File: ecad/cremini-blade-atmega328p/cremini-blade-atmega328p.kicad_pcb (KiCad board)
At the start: 2 copper layers, 25 x 99 mm, 96 parts, among them J1 USB-C PORT, J2 ICSP, J3 BACKPLANE, J4 RASPBERRY PI GPIO, Q1 AO3400A, Q2 AO3400A, Q3 SI2301CDS-T1-GE3, Q4 AO3400A, SW1 RESET, SW2 SW_DIP_x06, U1 ACS712ELCTR-20A-T, U2 ACS712ELCTR-20A-T, U3 LM358D, U4 CH340G, U5 AMS1117-3.3, U6 ATMEGA328P-AU, U7 74HC244D, Y1 12MHz, Y2 16MHz

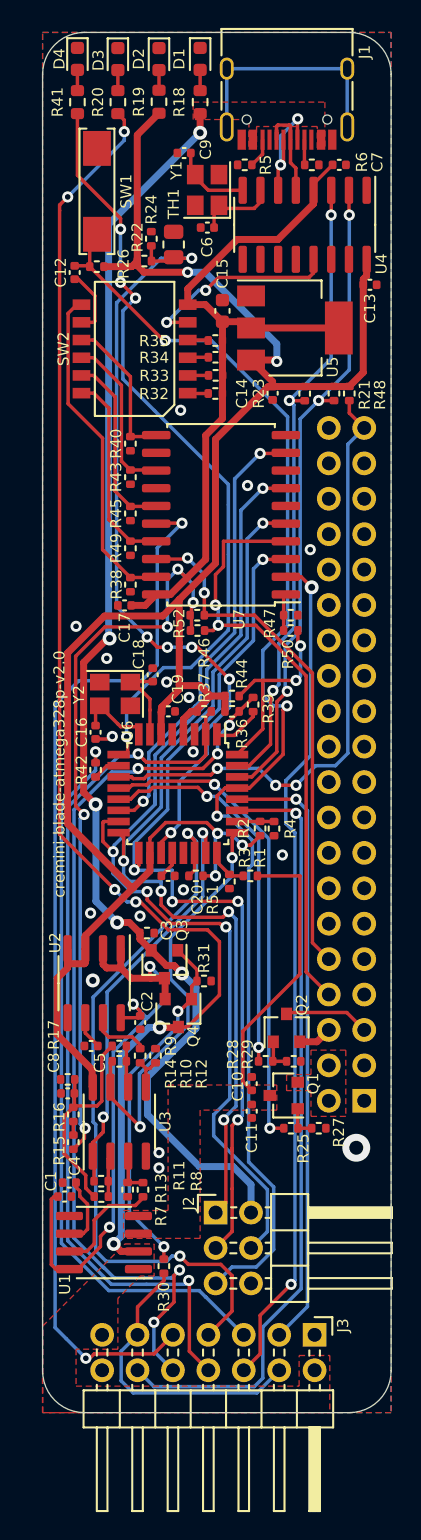
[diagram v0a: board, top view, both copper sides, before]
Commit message: Reroute PCB for backpower protection circuit
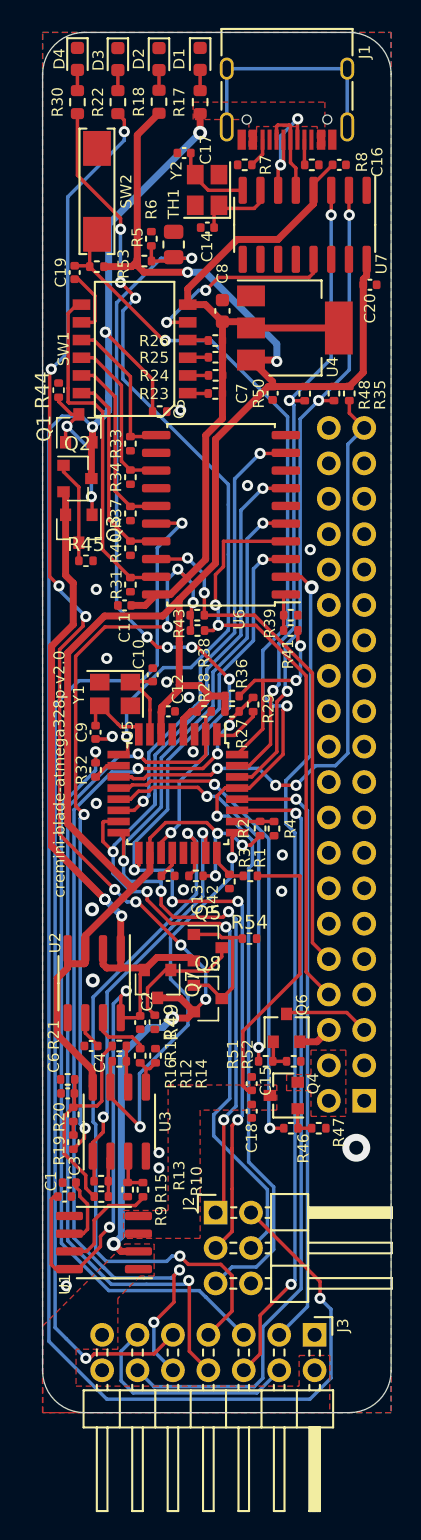
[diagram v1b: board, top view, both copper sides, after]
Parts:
- removed the Q4 at (106.7, 120.3)
- removed the R30 at (105.7, 138.5)
- removed the R31 at (108.6, 118.0)
- added Q1: Q_PNP_BEC, Package_TO_SOT_SMD:SOT-23, F.Cu at (99.6, 78.4)
- added Q2: AO3401A, Package_TO_SOT_SMD:SOT-23, F.Cu at (99.5, 82.0)
- added Q5: Q_PNP_BEC, Package_TO_SOT_SMD:SOT-23, F.Cu at (108.8, 115.7)
- added Q7: AO3401A, Package_TO_SOT_SMD:SOT-23, F.Cu at (105.2, 118.2)
- added Q8: Q_PNP_BEC, Package_TO_SOT_SMD:SOT-23, F.Cu at (108.8, 119.3)
- added R44: 20k, Resistor_SMD:R_0402_1005Metric, F.Cu at (98.2, 75.7)
- added R45: 100k, Resistor_SMD:R_0402_1005Metric, F.Cu at (100.1, 87.9)
- added R49: 100k, Resistor_SMD:R_0402_1005Metric, F.Cu at (105.0, 121.0)
- added R54: 20k, Resistor_SMD:R_0402_1005Metric, F.Cu at (111.8, 115.0)
- Q3: value SI2301CDS-T1-GE3 -> Q_PNP_BEC
- moved C5 37.4 mm to (105.4, 77.2)
- moved Q3 31.8 mm to (99.6, 85.6)
- turned C15 to 90 degrees
- renumbered C18 to C10, C17 to C11, C19 to C12, C20 to C13, C6 to C14, C10 to C15, C7 to C16, C9 to C17, C11 to C18, C12 to C19, C13 to C20, C4 to C3, C5 to C4, C3 to C5, C8 to C6, C14 to C7, C15 to C8, C16 to C9, Q1 to Q4, Q2 to Q6, R8 to R10, R9 to R11, R10 to R12, R11 to R13, R12 to R14, R13 to R15, R14 to R16, R18 to R17, R19 to R18, R15 to R19, R16 to R20, R17 to R21, R20 to R22, R32 to R23, R33 to R24, R34 to R25, R35 to R26, R36 to R27, R37 to R28, R39 to R29, R41 to R30, R38 to R31, R42 to R32, R40 to R33, R43 to R34, R48 to R35, R44 to R36, R45 to R37, R46 to R38, R47 to R39, R49 to R40, R50 to R41, R51 to R42, R52 to R43, R25 to R46, R27 to R47, R21 to R48, R22 to R5, R23 to R50, R28 to R51, R29 to R52, R26 to R53, R24 to R6, R5 to R7, R6 to R8, R7 to R9, SW2 to SW1, SW1 to SW2, U5 to U4, U6 to U5, U7 to U6, U4 to U7, Y2 to Y1, Y1 to Y2
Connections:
- net MISO renamed CIPO
- net MOSI renamed COPI
- net SCLK renamed SCK
- net VIN renamed RSV
- C15 pad 1: GND -> 5VSBC
- C15 pad 2: 5VSBC -> GND
- Q3 pad 2: 5VEXT -> 5VBMC
- Q3 pad 3: 5VBMC -> Net-(Q2-Pad1)
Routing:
- net 5VEXT: track 92.8 -> 142.8 mm, vias 5 -> 4
- net 5VBMC: track 45.7 -> 81.2 mm, vias 3 -> 5
- net Net-(Q1-Pad1): track 25.8 -> 11.6 mm
- net Net-(Q5-Pad1): track 0.00 -> 10.9 mm
- net Net-(Q5-Pad3): track 0.00 -> 9.13 mm
- net Net-(Q2-Pad1): track 0.00 -> 7.31 mm
- net RSV: track 21.4 -> 16.2 mm
- net 5VPSU: track 96.9 -> 99.3 mm, vias 6 -> 10
- net Net-(R31-Pad2): track 23.9 -> 24.9 mm
- net GND: vias 17 -> 19

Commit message: Fix silk screen and export latest STEP file
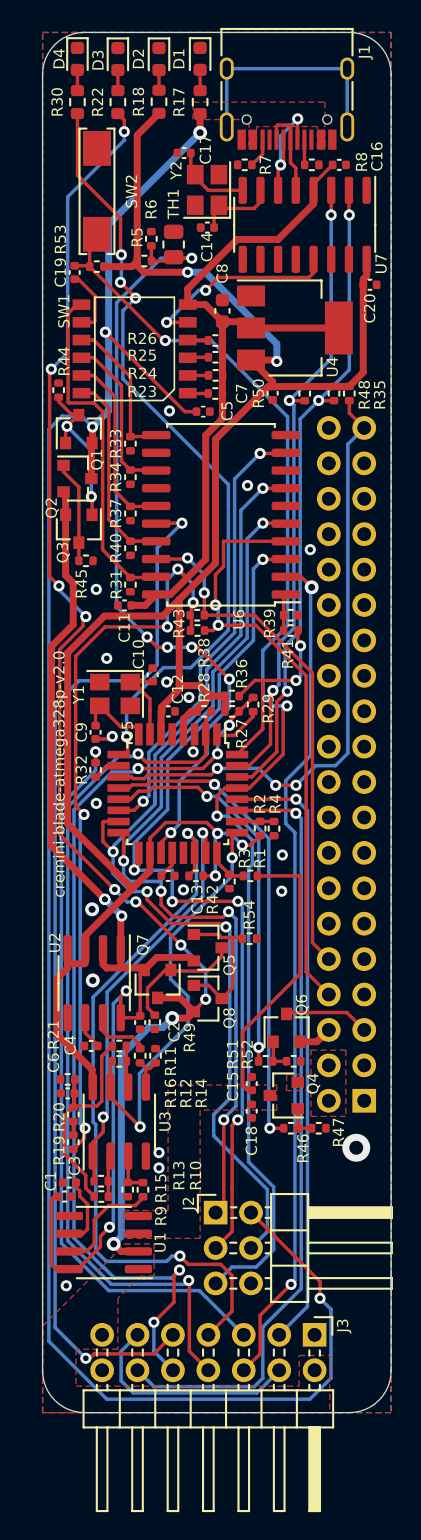
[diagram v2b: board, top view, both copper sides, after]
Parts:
- C5: footprint Resistor_SMD:R_0402_1005Metric -> Capacitor_SMD:C_0402_1005Metric
- SW1: footprint Mycelium:DIP_SW_x06 -> mykilio:DIP_SW_x06
- moved C5 3.12 mm to (108.5, 77.2)
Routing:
- net 5VEXT: track 142.8 -> 144.6 mm

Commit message: Update schematic of blade with reserved pins
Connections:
- J3 pad 11: RSV -> (no net)
- J3 pad 4: RSV -> (no net)
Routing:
- net RSV: track 16.2 -> 0.00 mm
